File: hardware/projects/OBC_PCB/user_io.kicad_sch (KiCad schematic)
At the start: 24 parts, among them J5 TC2030-CTX-NL, SW1 PREV, SW2 NEXT, SW3 SELECT / POWER, SW4 BACK, U10 SN74LVC2G00DCTR

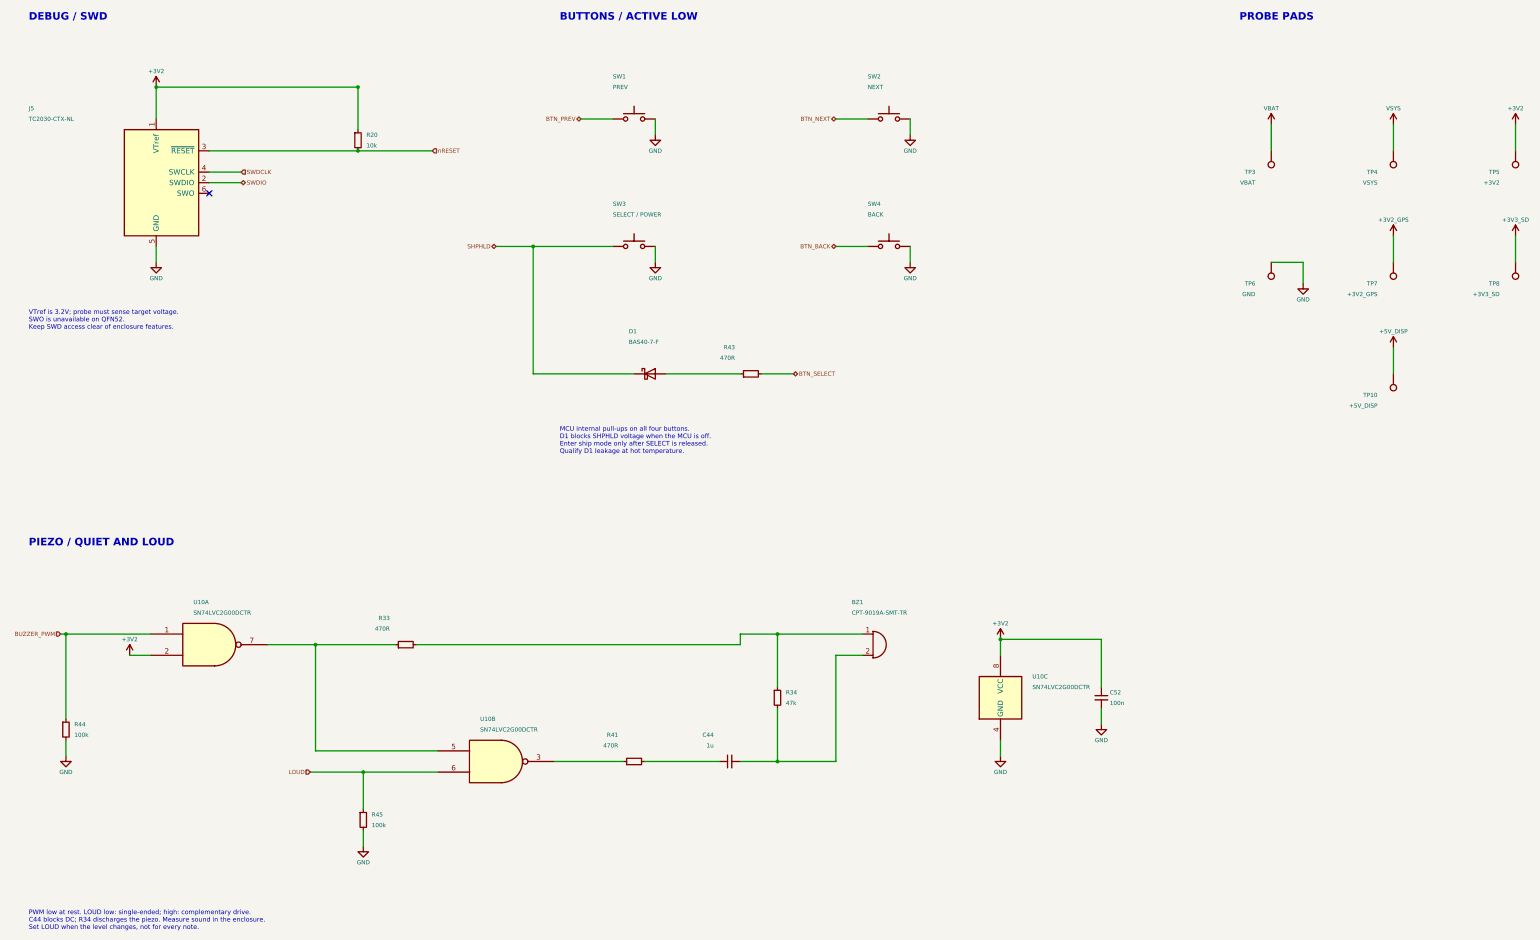
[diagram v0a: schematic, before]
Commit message: hardware: tidy the QFN schematic layout and style
Layout pass on the eight sheets. ERC stays at 0 violations on OBC_PCB and
USB_Baseboard. A netlist comparison shows the same 127 net partitions and
the same components, values and footprints.

Root sheet
- Draw SCL, SDA, COM_EN, LOUD, SHPHLD, BTN_SELECT and BUZZER_PWM as label
  stubs. Wire crossings fall from 38 to 0.
- Redraw the DCC/DECD/DECA/DECRF network as a chain without crossings.
- Move R5 and C26 clear of the crystal wires. Use a ground symbol on Y1
  instead of a label named GND.
- Hang the I2C test points on the U6C stubs.

Power sheet
- Attach the VBUS, VBAT and GND power flags to their nets.
- Tap TP1 onto the SHPHLD wire.
- Use a +3V2 symbol on LSIN2 instead of a label.
- Route SW2, the VSET straps and the CFG resistors without crossings.
- Move the SEL ground away from the LX1 pin.
- Show LSOUT1(GND) and INT(GND) for the unused LS1 and BMP581 pins.

Display, GNSS, user I/O
- Move J1 pin VA below VB so the VCOM/VB link no longer crosses VA.
- Move the GNSS FTE labels clear of the antenna pin 3 wire.
- Straighten the piezo wiring. Put the GND probe pad above its ground
  symbol.

Style
- One heading size (1.8 bold), one sub-heading size (1.27 bold) and one
  note size (1.0).
- Hide the voltage, dielectric and tolerance fields on the GNSS and radio
  sheets. Remove their dashed frames. Move both sheets to the top-left.
- Use Rev QFN and the same title format on every sheet.
- Set TP1 and TP2 to in_bom no like the other probe pads.
- Add C21 to the VDD bypass note.

Net names change for five nets because their labels are now on the root
sheet: BTN_SELECT, BUZZER_PWM, COM_EN, LOUD and SHPHLD. No net class
pattern uses them.

Co-Authored-By: Claude Sonnet 5.5 <noreply@anthropic.com>
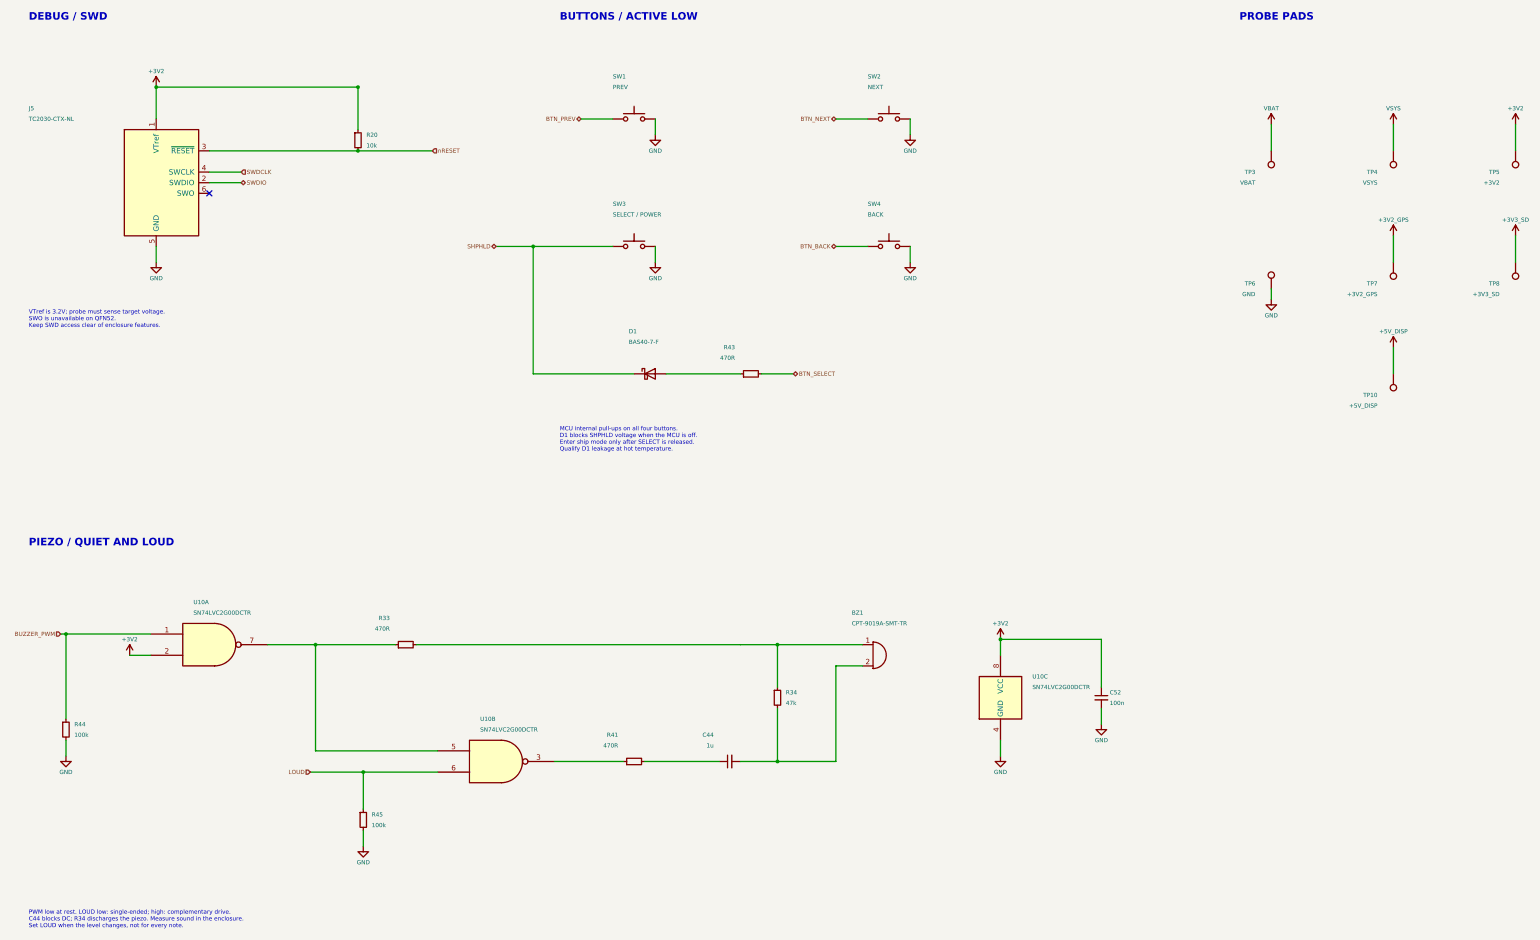
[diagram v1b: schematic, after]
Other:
- moved on the sheet: BZ1, TP6
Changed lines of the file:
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@@
 		(effects
 			(font
-				(size 1.1 1.1)
+				(size 1.0 1.0)
 			)
 			(justify left top)
@@
 		(effects
 			(font
-				(size 1.1 1.1)
+				(size 1.0 1.0)
 			)
 			(justify left top)
@@
 	(symbol
 		(lib_id "obc:CPT-9019A-SMT-TR")
-		(at 222.25 171.45 0)
+		(at 222.25 173.99 0)
 		(unit 1)
 		(exclude_from_sim no)
@@
 		(dnp no)
 		(property "Value" "CPT-9019A-SMT-TR"
-			(at 217.17 163.82999999999998 0)
+			(at 217.17 166.37 0)
 			(effects
 				(font
@@
 		)
 		(property "Footprint" "obc:CPT-9019A-SMT-TR"
-			(at 0 0 0)
+			(at 0 2.54 0)
 			(hide yes)
 			(effects
@@
 		)
 		(property "Datasheet" "https://www.sameskydevices.com/product/resource/cpt-9019a-smt-tr.pdf"
-			(at 0 0 0)
+			(at 0 2.54 0)
 			(hide yes)
 			(effects
@@
 		)
 		(property "Description" "Externally driven non-polar piezo transducer, 9x9x1.9mm, 4kHz"
-			(at 0 0 0)
+			(at 0 2.54 0)
 			(hide yes)
 			(effects
@@
 		)
 		(property "MPN" "CPT-9019A-SMT-TR"
-			(at 0 0 0)
+			(at 0 2.54 0)
 			(hide yes)
 			(effects
@@
 		)
 		(property "Manufacturer" "Same Sky"
-			(at 0 0 0)
+			(at 0 2.54 0)
 			(hide yes)
 			(effects
@@
 		)
 		(property "Rated Drive" "3Vpp, 4kHz, 50% square wave"
-			(at 0 0 0)
+			(at 0 2.54 0)
 			(hide yes)
 			(effects
@@
 		)
 		(property "Sound Pressure" "72dB min at 10cm, rated drive"
-			(at 0 0 0)
+			(at 0 2.54 0)
 			(hide yes)
 			(effects
@@
 		)
 		(property "Capacitance" "12nF +/-30%"
-			(at 0 0 0)
+			(at 0 2.54 0)
 			(hide yes)
 			(effects
@@
 		)
 		(property "Operating Voltage" "1 to 25Vpp"
-			(at 0 0 0)
+			(at 0 2.54 0)
 			(hide yes)
 			(effects
@@
 		)
 		(property "Operating Temperature" "-40 to +85 C"
-			(at 0 0 0)
+			(at 0 2.54 0)
 			(hide yes)
 			(effects
@@
 		)
 		(property "Reference" "BZ1"
-			(at 217.17 161.28999999999996 0)
+			(at 217.17 163.83 0)
 			(effects
 				(font
@@
 	(wire
 		(pts
-			(xy 190.5 171.45)
-			(xy 190.5 168.91)
-		)
-		(stroke
-			(width 0)
-			(type default)
-		)
-	)
-	(wire
-		(pts
-			(xy 190.5 168.91)
-			(xy 219.71 168.91)
-		)
-		(stroke
-			(width 0)
-			(type default)
-		)
-	)
-	(wire
-		(pts
 			(xy 190.5 199.39)
 			(xy 213.36 199.39)
@@
 		)
 	)
-	(wire
-		(pts
-			(xy 213.36 199.39)
-			(xy 213.36 173.99)
-		)
-		(stroke
-			(width 0)
-			(type default)
-		)
-	)
-	(wire
-		(pts
-			(xy 213.36 173.99)
-			(xy 219.71 173.99)
-		)
-		(stroke
-			(width 0)
-			(type default)
-		)
-	)
 	(symbol
 		(lib_id "Device:R_Small")
@@
 	(wire
 		(pts
-			(xy 199.39 181.61)
-			(xy 199.39 168.91)
-		)
-		(stroke
-			(width 0)
-			(type default)
-		)
-	)
-	(junction
-		(at 199.39 168.91)
-		(diameter 0)
-		(color 0 0 0 0)
-	)
-	(wire
-		(pts
 			(xy 199.39 186.69)
 			(xy 199.39 199.39)
@@
 		(effects
 			(font
-				(size 1.1 1.1)
+				(size 1.0 1.0)
 			)
 			(justify left top)
@@
 	(symbol
 		(lib_id "Connector:TestPoint")
-		(at 317.5 80.01 180)
+		(at 317.5 86.36 0)
 		(unit 1)
 		(exclude_from_sim no)
@@
 		(dnp no)
 		(property "Footprint" "TestPoint:TestPoint_Pad_D1.0mm"
-			(at 0 0 0)
+			(at 0 6.35 0)
 			(hide yes)
 			(effects
@@
 		)
 		(property "Datasheet" ""
-			(at 0 0 0)
+			(at 0 6.35 0)
 			(hide yes)
 			(effects
@@
 		)
 		(property "Description" "Bare 1mm probe pad for GND; no fitted part or solder paste"
-			(at 0 0 0)
+			(at 0 6.35 0)
 			(hide yes)
 			(effects
@@
 					(size 1 1)
 				)
-				(justify left)
+				(justify right)
 			)
 		)
 		(property "Value" "GND"
-			(at 313.69 87.63000000000001 0)
+			(at 313.69 87.63 0)
 			(effects
 				(font
 					(size 1 1)
 				)
-				(justify left)
+				(justify right)
 			)
 		)
@@
 	(symbol
 		(lib_id "power:GND")
-		(at 325.12 85.09 0)
+		(at 317.5 88.9 0)
 		(unit 1)
 		(exclude_from_sim no)
@@
 		(dnp no)
 		(property "Reference" "#PWR9000033"
-			(at 320.04 74.93 0)
+			(at 312.42 78.74 0)
 			(hide yes)
 			(show_name no)
@@
 		)
 		(property "Value" "GND"
-			(at 325.12 88.9 0)
+			(at 317.5 92.71 0)
 			(show_name no)
 			(do_not_autoplace no)
@@
 		)
 		(property "Footprint" ""
-			(at 7.62 11.43 0)
+			(at 0 15.24 0)
 			(hide yes)
 			(show_name no)
@@
 		)
 		(property "Datasheet" ""
-			(at 7.62 11.43 0)
+			(at 0 15.24 0)
 			(hide yes)
 			(show_name no)
@@
 		)
 		(property "Description" "Power symbol creates a global label with name \"GND\" , ground"
-			(at 7.62 11.43 0)
+			(at 0 15.24 0)
 			(hide yes)
 			(show_name no)
@@
 		)
 		(property "ki_keywords" "global power"
-			(at 7.62 11.43 0)
+			(at 0 15.24 0)
 			(hide yes)
 			(show_name no)
@@
 	(wire
 		(pts
-			(xy 317.5 80.01)
-			(xy 325.12 80.01)
+			(xy 190.5 171.45)
+			(xy 219.71 171.45)
+		)
+		(stroke
+			(width 0)
+			(type default)
+		)
+	)
+	(junction
+		(at 199.39 171.45)
+		(diameter 0)
+		(color 0 0 0 0)
+	)
+	(wire
+		(pts
+			(xy 199.39 181.61)
+			(xy 199.39 171.45)
+		)
+		(stroke
+			(width 0)
+			(type default)
+		)
+	)
+	(wire
+		(pts
+			(xy 213.36 199.39)
+			(xy 213.36 176.53)
+		)
+		(stroke
+			(width 0)
+			(type default)
+		)
+	)
+	(wire
+		(pts
+			(xy 213.36 176.53)
+			(xy 219.71 176.53)
 		)
 		(stroke
@@
 	(wire
 		(pts
-			(xy 325.12 80.01)
-			(xy 325.12 85.09)
+			(xy 317.5 86.36)
+			(xy 317.5 88.9)
 		)
 		(stroke

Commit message: hardware: consolidate capacitor parts
One part per value and footprint where the ratings allow it:

- 1 uF 0603 (C6, C14, C20, C44, C54): 25 V X7R, 10 %. Three ratings and
  two dielectrics become one part.
- 100 nF 0402 (17 parts): 10 V X7R, 10 %. C7, C16 and C17 move from X5R.
- 2.2 uF 0603: C15 joins C39, C40 and C49 at 16 V X7R.
- Descriptions, tolerances and ratings are now the same for every part of
  a value and footprint (2.2 uF 0402, 10 uF 0603, 10 uF 0805, generic
  descriptions on C51 to C54).

Four capacitor BOM lines fewer. The higher-rated X7R parts lose less
capacitance under DC bias than the X5R parts they replace. A 25 V 1 uF
0603 costs about 1 cent more than a 10 V one at 10 pieces.

ERC stays at 0 violations and the netlist is unchanged.

Co-Authored-By: Claude Sonnet 5.5 <noreply@anthropic.com>
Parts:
- C44: Tolerance (none) -> 10%; Voltage 10V -> 25V
- C52: Tolerance (none) -> 10%
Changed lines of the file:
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@@
 			)
 		)
-		(property "Description" "1uF AC coupling capacitor, 10V, X7R"
+		(property "Description" "Ceramic MLCC, 1uF, 25V, X7R, 10%, 0603"
 			(at 0 0 0)
 			(hide yes)
@@
 			)
 		)
-		(property "Voltage" "10V"
+		(property "Voltage" "25V"
 			(at 0 0 0)
 			(hide yes)
@@
 				(font
 					(size 1 1)
+				)
+				(justify left)
+			)
+		)
+		(property "Tolerance" "10%"
+			(at 0 0 0)
+			(hide yes)
+			(effects
+				(font
+					(size 1.27 1.27)
 				)
 				(justify left)
@@
 			)
 		)
-		(property "Description" "Unpolarized capacitor, small symbol"
+		(property "Description" "Ceramic MLCC, 100nF, 10V, X7R, 10%, 0402"
 			(at 0 0 0)
 			(hide yes)
@@
 				)
 				(justify left)
+			)
+		)
+		(property "Tolerance" "10%"
+			(at 0 0 0)
+			(hide yes)
+			(effects
+				(font
+					(size 1.27 1.27)
+				)
+				(justify left)
